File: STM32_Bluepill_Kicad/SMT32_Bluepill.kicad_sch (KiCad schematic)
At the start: 2 parts, among them IC1 RT9193-33GB, U1 STM32F103C8Tx

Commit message: Schematic done, PCB 50%
Component placements still undone
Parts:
- added C1, C10, C11, C3, C4, C7, C8: 104_0603, PCM_Capacitor_SMD_AKL:C_0603_1608Metric, symbol PCM_Capacitor_AKL:C_0603
- added C12, C13, C14, C9: 20pF_0603, PCM_Capacitor_SMD_AKL:C_0603_1608Metric, symbol PCM_Capacitor_AKL:C_0603
- added C15: 223_0603, PCM_Capacitor_SMD_AKL:C_0603_1608Metric, symbol PCM_Capacitor_AKL:C_0603
- added C2: 105_0603, PCM_Capacitor_SMD_AKL:C_0603_1608Metric, symbol PCM_Capacitor_AKL:C_0603
- added C5: 105_0805, PCM_Capacitor_SMD_AKL:C_0805_2012Metric, symbol PCM_Capacitor_AKL:C_0805
- added C6: 106_0805, PCM_Capacitor_SMD_AKL:C_0805_2012Metric, symbol PCM_Capacitor_AKL:C_0805
- added D1: LED_0805_Red, PCM_LED_SMD_AKL:LED_0805_2012Metric, symbol PCM_LED_AKL:LED_0805_Red
- added D2: LED_0805_Blue, PCM_LED_SMD_AKL:LED_0805_2012Metric, symbol PCM_LED_AKL:LED_0805_Blue
- added P1: PINHD_2x3_Male, Connector_PinHeader_2.54mm:PinHeader_2x03_P2.54mm_Vertical, symbol PCM_SL_Pin_Headers:PINHD_2x3_Male
- added P2: PINHD_1x4_Male, Connector_PinHeader_2.54mm:PinHeader_1x04_P2.54mm_Vertical, symbol PCM_SL_Pin_Headers:PINHD_1x4_Male
- added P3, P4: PINHD_1x20_Male, Connector_PinHeader_2.54mm:PinHeader_1x20_P2.54mm_Vertical, symbol PCM_SL_Pin_Headers:PINHD_1x20_Male
- added R1, R5: 510_0603, PCM_Resistor_SMD_AKL:R_0603_1608Metric, symbol PCM_Resistor_AKL:R_0603
- added R10: 4K7_0603, PCM_Resistor_SMD_AKL:R_0603_1608Metric, symbol PCM_Resistor_AKL:R_0603
- added R11, R9: 20_0603, PCM_Resistor_SMD_AKL:R_0603_1608Metric, symbol PCM_Resistor_AKL:R_0603
- added R2: 10K_0603, PCM_Resistor_SMD_AKL:R_0603_1608Metric, symbol PCM_Resistor_AKL:R_0603
- added R3, R4: 100K_0603, PCM_Resistor_SMD_AKL:R_0603_1608Metric, symbol PCM_Resistor_AKL:R_0603
- added R6: 1M_0603, PCM_Resistor_SMD_AKL:R_0603_1608Metric, symbol PCM_Resistor_AKL:R_0603
- added RST1: Push_Button, Button_Switch_THT:SW_PUSH_6mm, symbol PCM_SL_Devices:Push_Button
- added U3: 10103593-0001LF, USBmicro_10103593-0001LF:AMPHENOL_10103593-0001LF, symbol USBmicro_10103593-0001LF:10103593-0001LF
- added Y2: Crystal_8MHz, Crystal:Crystal_HC49-4H_Vertical, symbol PCM_SL_Devices:Crystal_8MHz
- added Y3: Crystal_32.768kHz, Crystal:Crystal_AT310_D3.0mm_L10.0mm_Horizontal, symbol PCM_SL_Devices:Crystal_32.768kHz
- renumbered IC1 to U1, U1 to U2
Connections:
- net VBAT: now reaches U2.1 (VBAT)
- net VBAT: now also P4.1
- net PA0: now reaches U2.10 (PA0)
- net PA0: now also P4.5
- net PA1: now reaches U2.11 (PA1)
- net PA1: now also P4.6
- net PA2: now reaches U2.12 (PA2)
- net PA2: now also P4.7
- net PA3: now reaches U2.13 (PA3)
- net PA3: now also P4.8
- net PA4: now reaches U2.14 (PA4)
- net PA4: now also P4.9
- net PA5: now reaches U2.15 (PA5)
- net PA5: now also P4.10
- net PA6: now reaches U2.16 (PA6)
- net PA6: now also P4.11
- net PA7: now reaches U2.17 (PA7)
- net PA7: now also P4.12
- net PB0: now reaches U2.18 (PB0)
- net PB0: now also P4.13
- net PB1: now reaches U2.19 (PB1)
- net PB1: now also P4.14
- net PC13: now reaches U2.2 (PC13)
- net PC13: now also P4.2, R5.2
- net BOOT1: now reaches U2.20 (PB2)
- net BOOT1: now also R4.2
- net PB10: now reaches U2.21 (PB10)
- net PB10: now also P4.15
- net PB11: now reaches U2.22 (PB11)
- net PB11: now also P4.16
- net GND: now reaches U2.23 (VSS), U2.35 (VSS), U2.47 (VSS)
- net GND: now also U1.2 (GND), U2.8 (VSSA), C1.2, C10.2, C11.2, C12.1, C15.2, C2.2, C3.2, C4.2, C5.2, C6.2, C7.2, C8.2, C9.1, P1.5, P1.6, P2.4, P3.2, P4.19, P4.20, R1.1, RST1.1, U3.4 (ID), U3.5 (GND)
- net +3V3: now reaches U2.24 (VDD)
- net +3V3: now also U1.5 (VOUT), U2.36 (VDD), U2.48 (VDD), U2.9 (VDDA), C1.1, C10.1, C11.1, C3.1, C4.1, C6.1, C8.1, D1.2 (A), D2.2 (A), P1.1, P1.2, P2.1, P3.1, R2.1
- net PB12: now reaches U2.25 (PB12)
- net PB12: now also P3.20
- net PB13: now reaches U2.26 (PB13)
- net PB13: now also P3.19
- net PB14: now reaches U2.27 (PB14)
- net PB14: now also P3.18
- net PB15: now reaches U2.28 (PB15)
- net PB15: now also P3.17
- net PA8: now reaches U2.29 (PA8)
- net PA8: now also P3.16
- net PC14: now reaches U2.3 (PC14)
- net PC14: now also C9.2, P4.3, Y3.1
- net PA9: now reaches U2.30 (PA9)
- net PA9: now also P3.15
- net PA10: now reaches U2.31 (PA10)
- net PA10: now also P3.14
- net PA11: now reaches U2.32 (PA11)
- net PA11: now also P3.13, R9.2
- net PA12: now reaches U2.33 (PA12)
- net PA12: now also P3.12, R10.1, R11.2
- net SWDIO: now reaches U2.34 (PA13)
- net SWDIO: now also P2.2
- net SWDCLK: now reaches U2.37 (PA14)
- net SWDCLK: now also P2.3
- net PA15: now reaches U2.38 (PA15)
- net PA15: now also P3.11
- net PB3: now reaches U2.39 (PB3)
- net PB3: now also P3.10
- net PC15: now reaches U2.4 (PC15)
- net PC15: now also C12.2, P4.4, Y3.2
- net PB4: now reaches U2.40 (PB4)
- net PB4: now also P3.9
- net PB5: now reaches U2.41 (PB5)
- net PB5: now also P3.8
- net PB6: now reaches U2.42 (PB6)
- net PB6: now also P3.7
- net PB7: now reaches U2.43 (PB7)
- net PB7: now also P3.6
- net BOOT0: now reaches U2.44 (BOOT0)
- net BOOT0: now also R3.1
- net PB8: now reaches U2.45 (PB8)
- net PB8: now also P3.5
- net PB9: now reaches U2.46 (PB9)
- net PB9: now also P3.4
- net OSCIN: now reaches U2.5 (PD0)
- net OSCIN: now also C13.2, R6.2, Y2.1
- net OSCOUT: now reaches U2.6 (PD1)
- net OSCOUT: now also C14.2, R6.1, Y2.2
- net NRST: now reaches U2.7 (NRST)
- net NRST: now also P4.17
- net +5V: now reaches U1.1 (VIN)
- net +5V: now also U1.3 (EN), C5.1, C7.1, P3.3, R10.2, U3.1 (VCC)
- net at U1.4 (BP): now also C15.1
- new net: C2.1, R2.2, RST1.2
- new net: C13.1, C14.1
- new net: P1.3, R3.2
- new net: D2.1 (K), R5.1
- new net: R9.1, U3.2 (D-)
- new net: R11.1, U3.3 (D+)
- new net: P1.4, R4.1
- new net: D1.1 (K), R1.2
- new net 3V3: P4.18
- new net Earth: U3.S1 (SHIELD), U3.S2 (SHIELD), U3.S3 (SHIELD), U3.S4 (SHIELD), U3.S5 (SHIELD), U3.S6 (SHIELD)
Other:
- note added: "BOOT"
- note added: "LDO 5V -> 3V3"
- note added: "LED"
- note added: "RESET"
- moved on the sheet: U1, U2

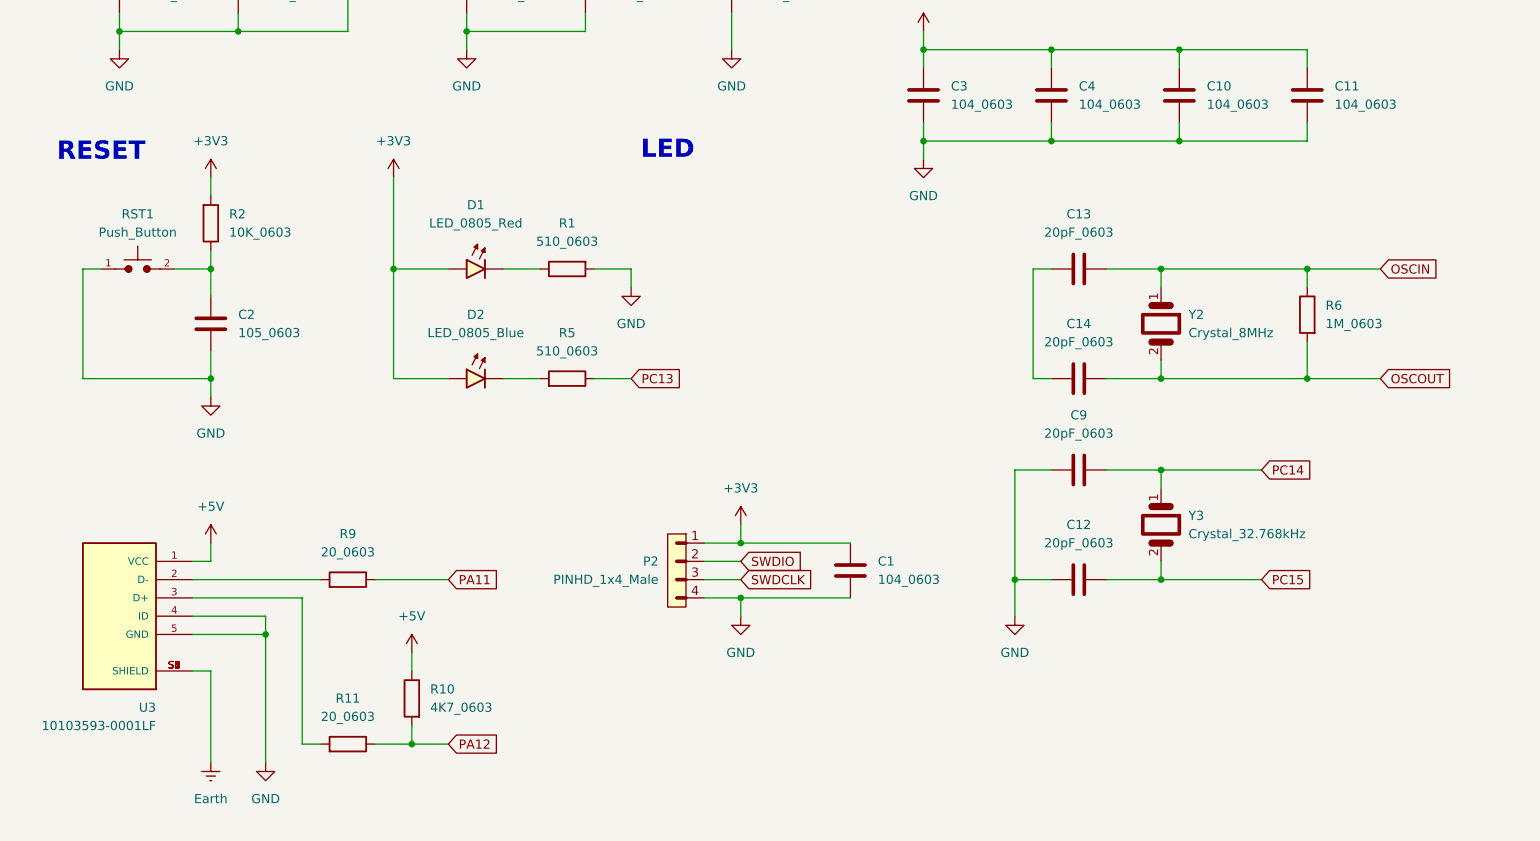
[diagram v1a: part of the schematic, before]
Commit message: PCB 70%
This version haven't been to redesign
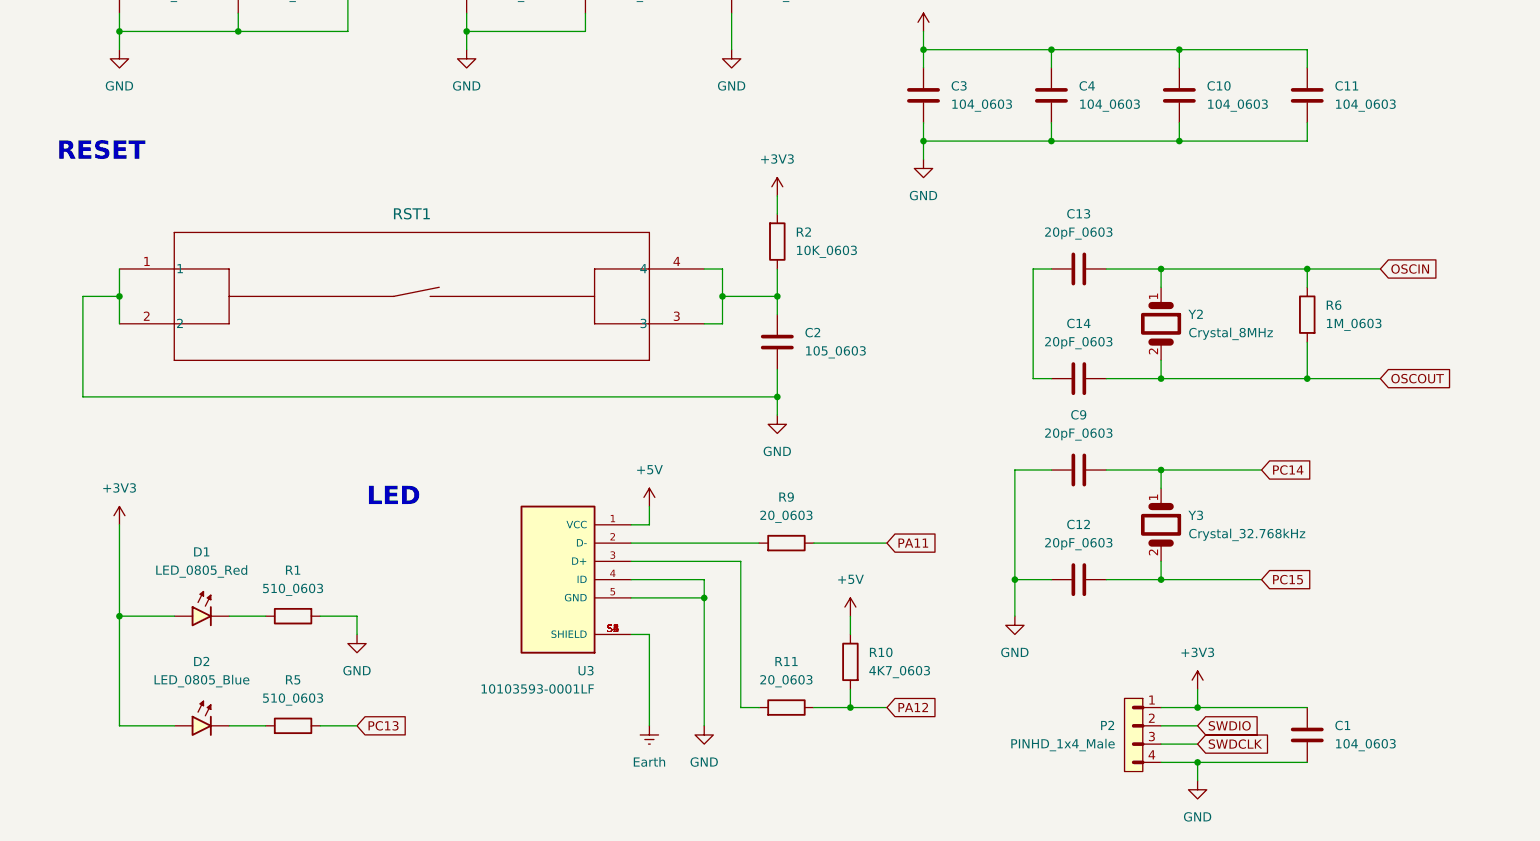
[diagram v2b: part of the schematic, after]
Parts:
- removed RST1: Push_Button, Button_Switch_THT:SW_PUSH_6mm, symbol PCM_SL_Devices:Push_Button
- added RST1: PTS526 SM15 SMTR2 LFS, SWST_PTS526_SM15_SMTR2_LFS:SON4_PTS526 SM15 SMTR2 LFS_CNK-M, symbol SWST_PTS526_SM15_SMTR2_LFS:PTS526_SM15_SMTR2_LFS
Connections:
- net GND: now also RST1.1, RST1.2
- net at C2.1, R2.2: now also RST1.3, RST1.4
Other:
- moved on the sheet: C1, C2, D1, D2, P2, R1, R10, R11, R2, R5, R9, U3

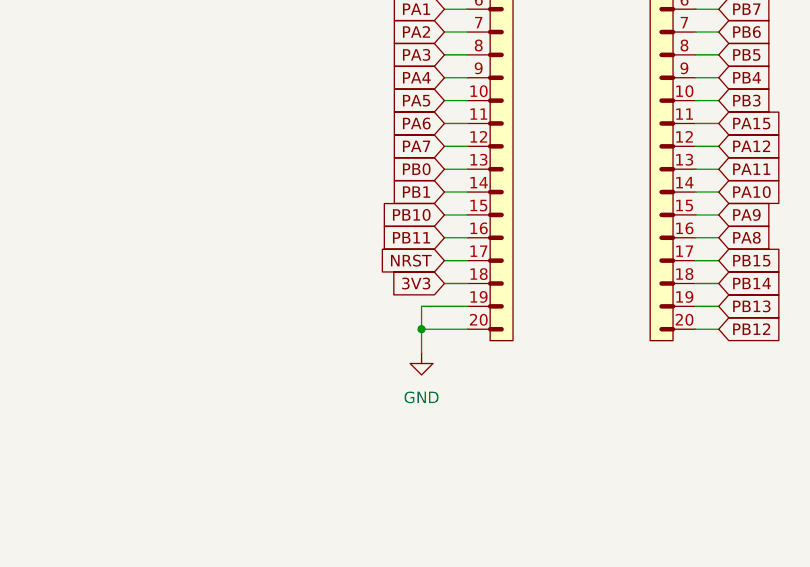
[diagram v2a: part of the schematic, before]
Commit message: PCB 80%
There are some traces that need to be retraced
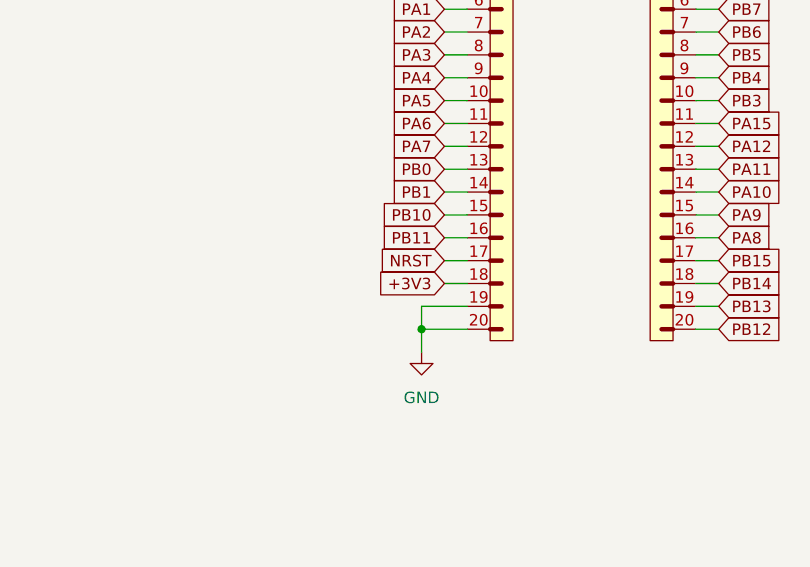
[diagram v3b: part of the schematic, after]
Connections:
- net 3V3 is gone; now on net +3V3: P4.18
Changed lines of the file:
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@@
 		)
 	)
-	(global_label "3V3"
+	(global_label "+3V3"
 		(shape input)
 		(at 353.06 68.58 180)
@@
 		)
 		(property "Intersheetrefs" "${INTERSHEET_REFS}"
-			(at 346.5672 68.58 0)
+			(at 344.9948 68.58 0)
 			(effects
 				(font
@@
 		(polyline
 			(pts
-				(xy 20.32 121.92) (xy 71.12 121.92) (xy 71.12 167.64) (xy 20.32 167.64)
-			)
-			(stroke
-				(width 0)
-				(type solid)
-			)
-			(fill
-				(type none)
-			)
-		)
-	)
-	(rule_area
-		(polyline
-			(pts
 				(xy 15.24 15.494) (xy 127 15.494) (xy 127 71.374) (xy 127 71.374) (xy 15.24 71.374)
 			)
@@
 			)
 			(fill
+				(type none)
+			)
+		)
+	)
+	(rule_area
+		(polyline
+			(pts
+				(xy 20.32 121.92) (xy 71.12 121.92) (xy 71.12 167.64) (xy 20.32 167.64)
+			)
+			(stroke
+				(width 0)
+				(type solid)
+			)
+			(fill

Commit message: Final R0
Done R0
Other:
- company: (none) -> muhardianab
- title: (none) -> STM32 Blue Pill
- moved on the sheet: C1, C10, C11, C12, C13, C14, C3, C4, C9, P2, P3, P4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
